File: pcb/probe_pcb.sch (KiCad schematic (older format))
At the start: 43 parts, among them J1 USB_B, J2 USB_B, J3 CONN_01X02, J4 CONN_01X02, J5 CONN_02X20, Q1 MMBT3904, Q2 MMBT3904, Q3 MMBT3904, Q4 MMBT3904, Q5 MMBT3904, Q6 MMBT3904, Q7 BC807-40, Q8 BC807-40, U1 ST_LINK, U2 ST_LINK, U3 ST_LINK, U4 TARGET, U5 TARGET, U6 TARGET, Y1 8MHz

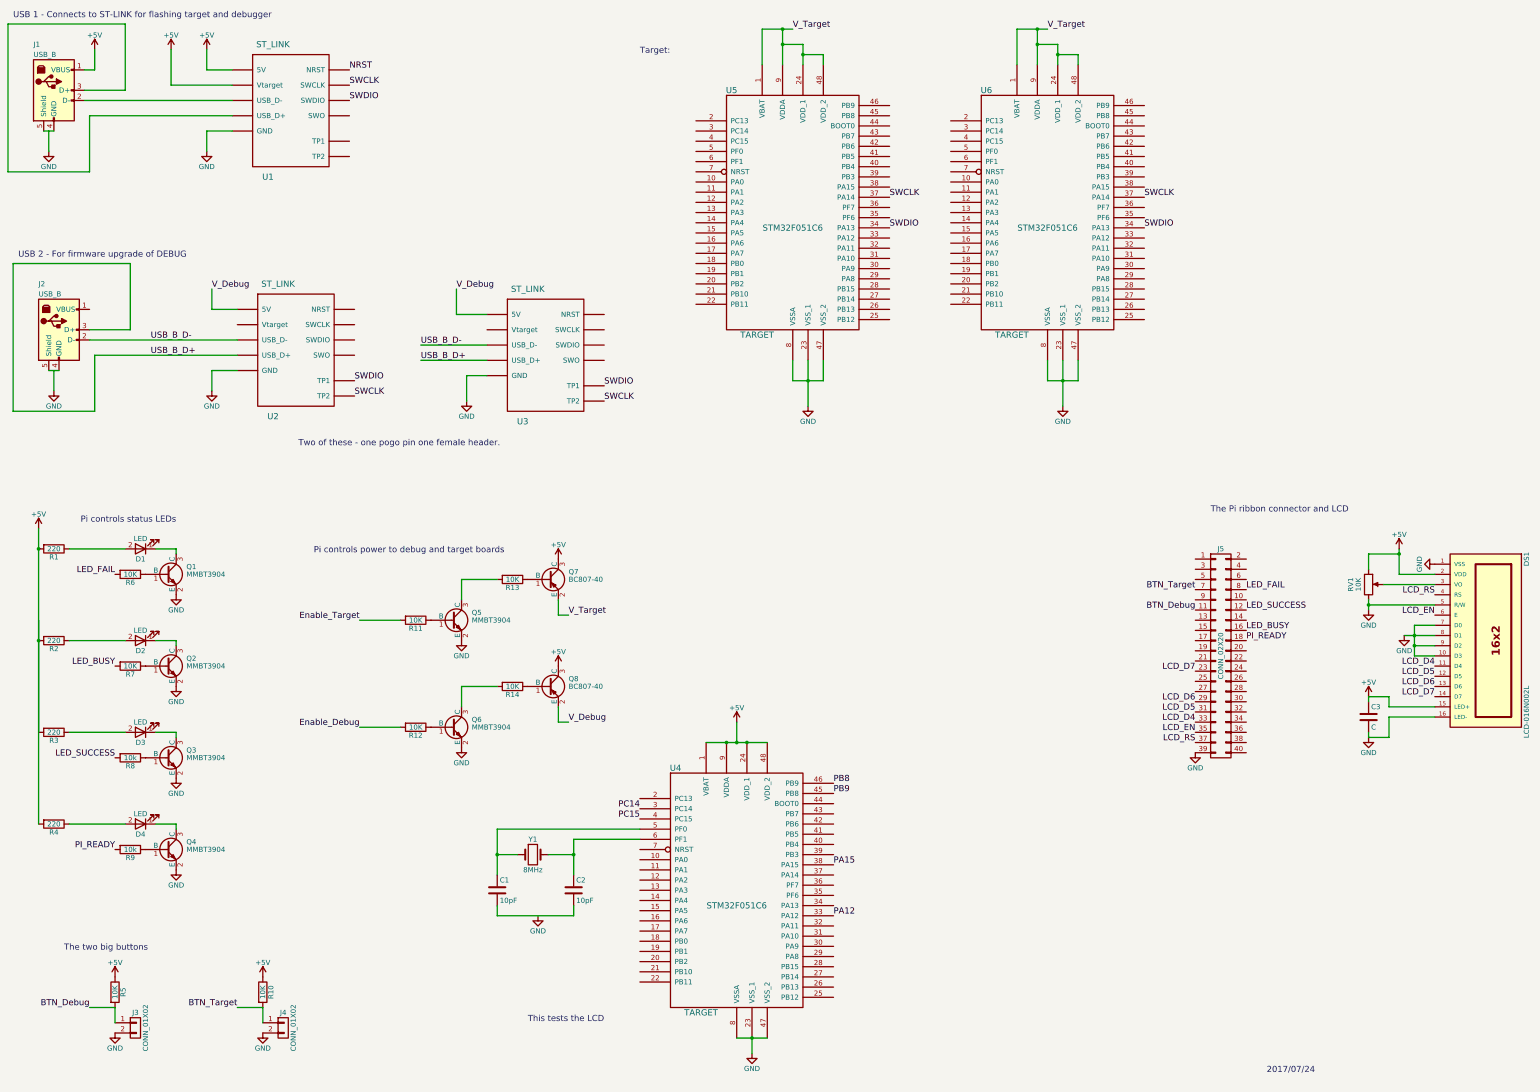
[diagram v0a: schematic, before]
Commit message: Now with three LCDs. Duplicate circuitry though, which needs removal!
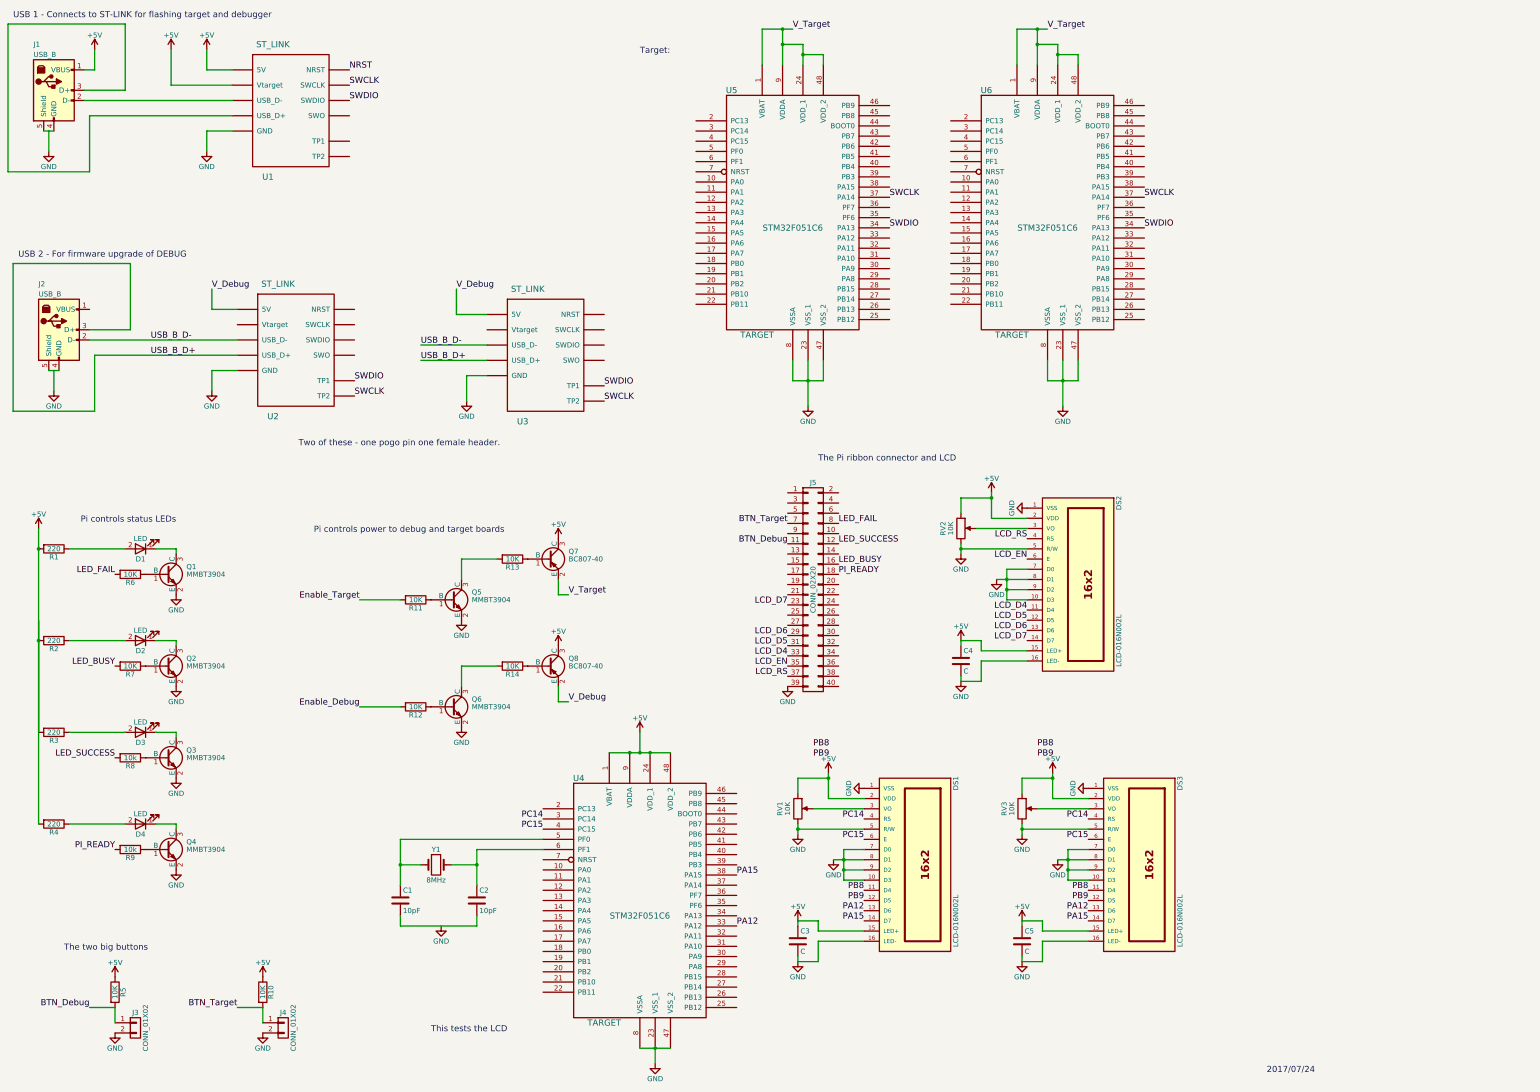
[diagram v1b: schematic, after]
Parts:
- added C4, C5: C, symbol C
- added DS2, DS3: LCD-016N002L, WC1602A, symbol LCD-016N002L
- added RV2, RV3: 10K, symbol POT
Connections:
- net +5V: now also C4.1, C5.1, DS2.15 (LED+), DS2.2 (VDD), DS3.15 (LED+), DS3.2 (VDD), RV2.1, RV3.1
- net GND: now also C4.2, C5.2, DS2.1 (VSS), DS2.10 (D3), DS2.16 (LED-), DS2.5 (R/W), DS2.7 (D0), DS2.8 (D1), DS2.9 (D2), DS3.1 (VSS), DS3.10 (D3), DS3.16 (LED-), DS3.5 (R/W), DS3.7 (D0), DS3.8 (D1), DS3.9 (D2), RV2.3, RV3.3
- net LCD_D4: now also DS2.11 (D4); no longer DS1.11 (D4)
- net LCD_D5: now also DS2.12 (D5); no longer DS1.12 (D5)
- net LCD_D6: now also DS2.13 (D6); no longer DS1.13 (D6)
- net LCD_D7: now also DS2.14 (D7); no longer DS1.14 (D7)
- net LCD_EN: now also DS2.6 (E); no longer DS1.6 (E)
- net LCD_RS: now also DS2.4 (RS); no longer DS1.4 (RS)
- net PA12: now also DS1.13 (D6), DS3.13 (D6)
- net PA15: now also DS1.14 (D7), DS3.14 (D7)
- net PB8: now also DS1.11 (D4), DS3.11 (D4); no longer U4.46 (PB9)
- net PB9: now also DS1.12 (D5), DS3.12 (D5); no longer U4.45 (PB8)
- net PC14: now also DS1.4 (RS), DS3.4 (RS)
- net PC15: now also DS1.6 (E), DS3.6 (E)
- new net: DS2.3 (VO), RV2.2
- new net: DS3.3 (VO), RV3.2
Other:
- moved on the sheet: C1, C2, C3, DS1, J5, Q5, Q6, Q7, Q8, R11, R12, R13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

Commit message: Cleaned up LCD test circuit.
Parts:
- removed C5: C, symbol C
- removed RV3: 10K, symbol POT
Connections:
- net PB8: now also U4.45 (PB8)
- net PB9: now also U4.46 (PB9)
- net VO: now reaches DS1.3 (VO), RV1.2
- net VO: now also DS3.3 (VO)
